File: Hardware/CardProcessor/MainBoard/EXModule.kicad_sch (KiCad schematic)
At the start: 1 part, among them J3 MEC5-140-01-L-DV-W1-K

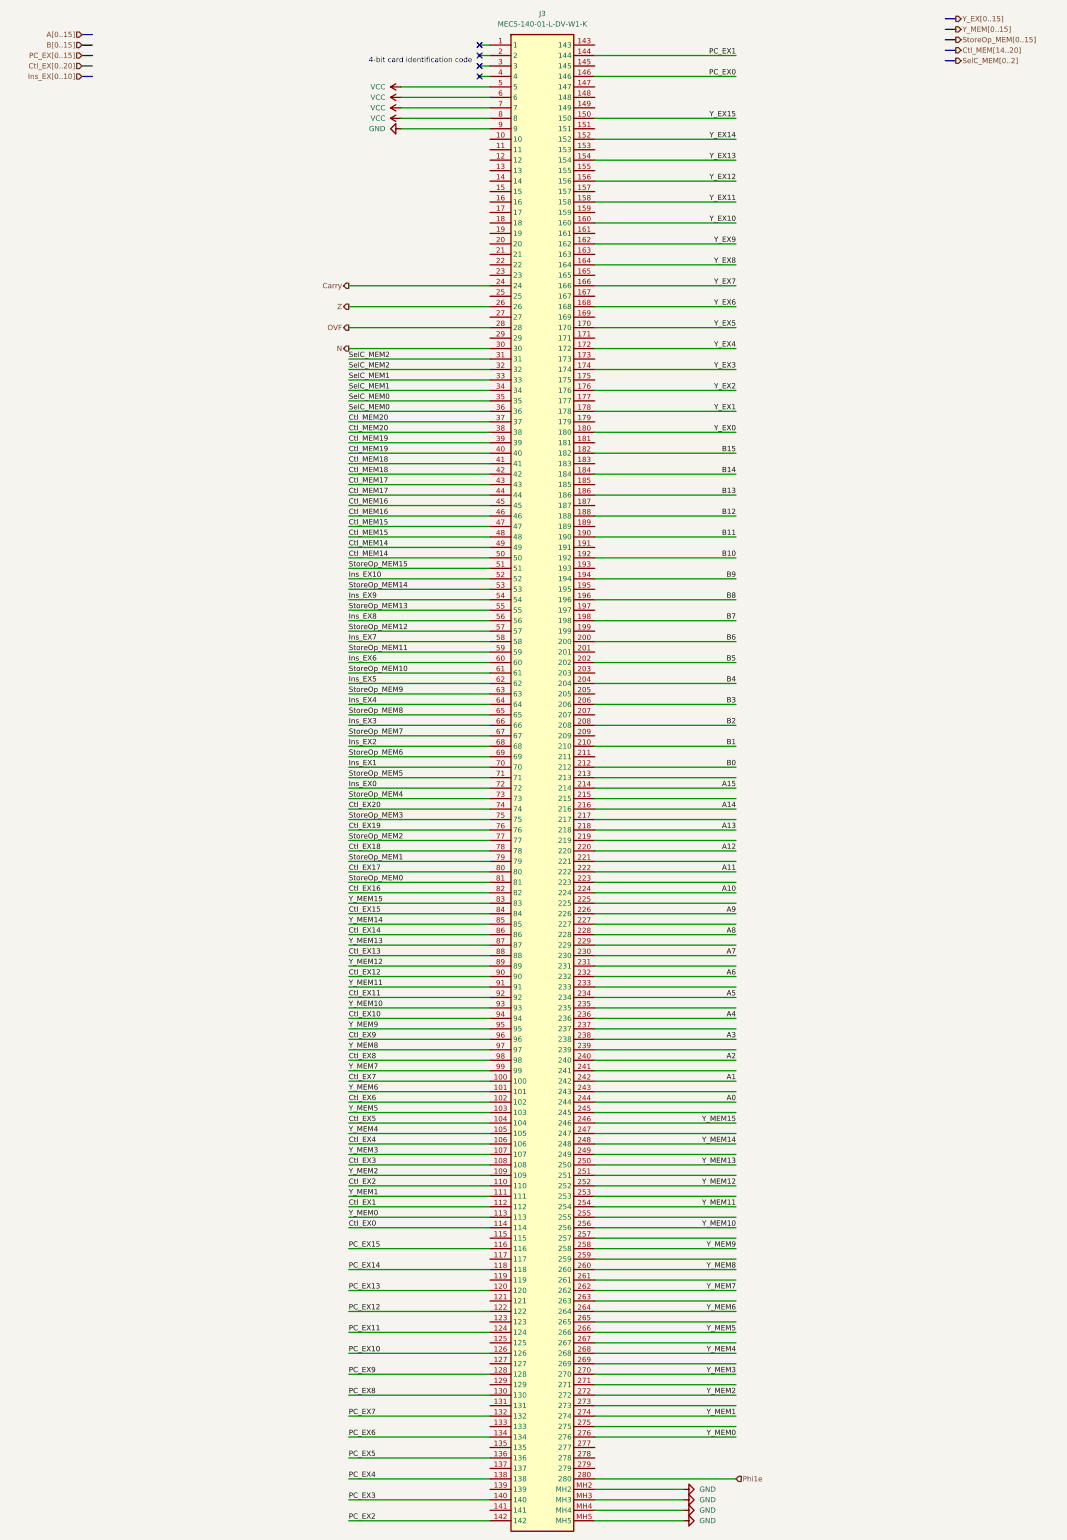
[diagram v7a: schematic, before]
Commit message: MainBoard: unconnected fingers on the edge connectors are grounded
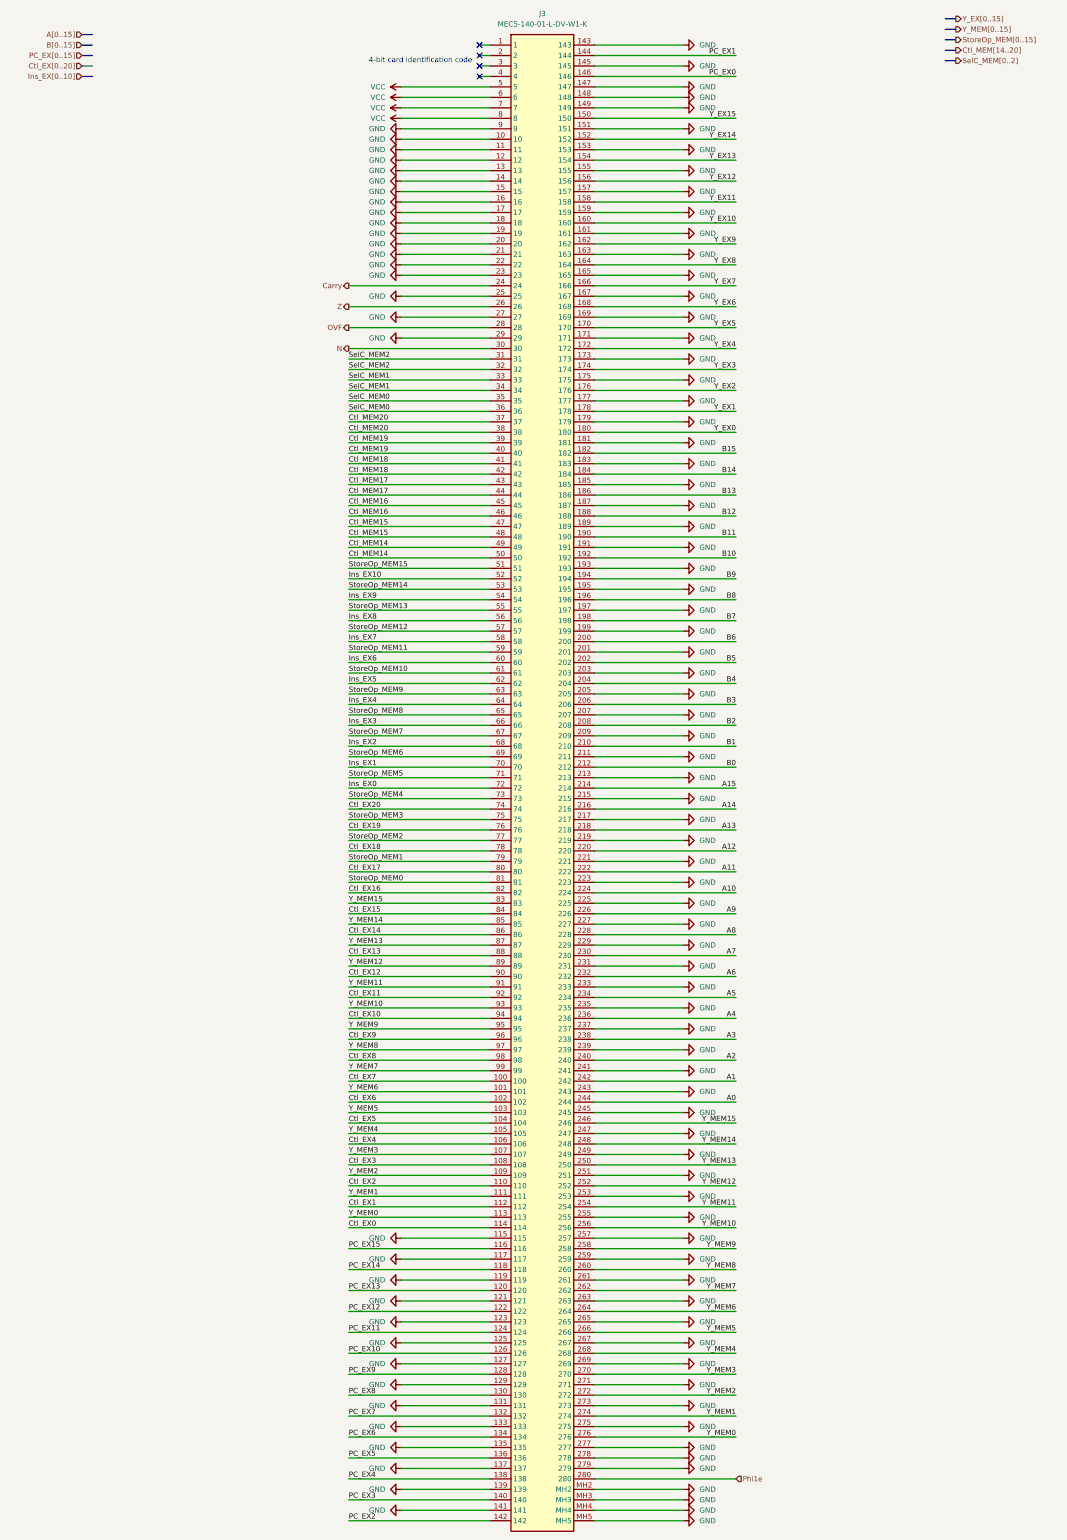
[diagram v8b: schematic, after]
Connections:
- net GND: now also J3.10, J3.11, J3.115, J3.117, J3.119, J3.12, J3.121, J3.123, J3.125, J3.127, J3.129, J3.13, J3.131, J3.133, J3.135, J3.137, J3.139, J3.14, J3.141, J3.143, J3.145, J3.147, J3.148, J3.149, J3.15, J3.151, J3.153, J3.155, J3.157, J3.159, J3.16, J3.161, J3.163, J3.165, J3.167, J3.169, J3.17, J3.171, J3.173, J3.175, J3.177, J3.179, J3.18, J3.181, J3.183, J3.185, J3.187, J3.189, J3.19, J3.191, J3.193, J3.195, J3.197, J3.199, J3.20, J3.201, J3.203, J3.205, J3.207, J3.209, J3.21, J3.211, J3.213, J3.215, J3.217, J3.219, J3.22, J3.221, J3.223, J3.225, J3.227, J3.229, J3.23, J3.231, J3.233, J3.235, J3.237, J3.239, J3.241, J3.243, J3.245, J3.247, J3.249, J3.25, J3.251, J3.253, J3.255, J3.257, J3.259, J3.261, J3.263, J3.265, J3.267, J3.269, J3.27, J3.271, J3.273, J3.275, J3.277, J3.278, J3.279, J3.29
